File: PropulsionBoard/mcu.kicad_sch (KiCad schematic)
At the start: 22 parts, among them J3 Programming Header, U11 PIC18F26K83, U12 MC2562, Y1 Crystal

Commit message: Address Jack's comment on the propulsion board
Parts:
- removed IC1: ~, PropulsionBoard:QFN24_4MM_SMSC, symbol PropulsionBoard-eagle-import:PCF8575
- removed R42: 230R, Resistor_SMD:R_0805_2012Metric_Pad1.20x1.40mm_HandSolder, symbol Device:R_US
- removed R43, R44: 500R, Resistor_SMD:R_0805_2012Metric_Pad1.20x1.40mm_HandSolder, symbol Device:R_US
- added R13: 150R, Resistor_SMD:R_0805_2012Metric_Pad1.20x1.40mm_HandSolder, symbol Device:R_US
- added R14, R52: 330R, Resistor_SMD:R_0805_2012Metric_Pad1.20x1.40mm_HandSolder, symbol Device:R_US
- added U5: PCA9536DR, D8, symbol 2023-11-18_21-56-52:PCA9536DR
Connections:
- net +3V3: now also C17.2, J3.4 (Pin_4), R41.1, U11.20 (VDD), U12.5 (VIO), R13.1, R14.1, R52.1, U5.8 (VCC)
- net +5V: no longer C17.2, J3.4 (Pin_4), R41.1, U11.20 (VDD), U12.5 (VIO)
- net GND: now also U5.4 (GND)
- net SCL: now also U5.6 (SCL)
- net SDA: now also U5.7 (SDA)
- net at D1.2 (A): now also R13.2
- net at D2.2 (A): now also R14.2
- net at D3.2 (A): now also R52.2
- new net VALVE_CONTROL 1: U5.1 (P0)
- new net VALVE_CONTROL 2: U5.2 (P1)
- new net VALVE_CONTROL 3: U5.3 (P2)
- no-connect marks 0 -> 3

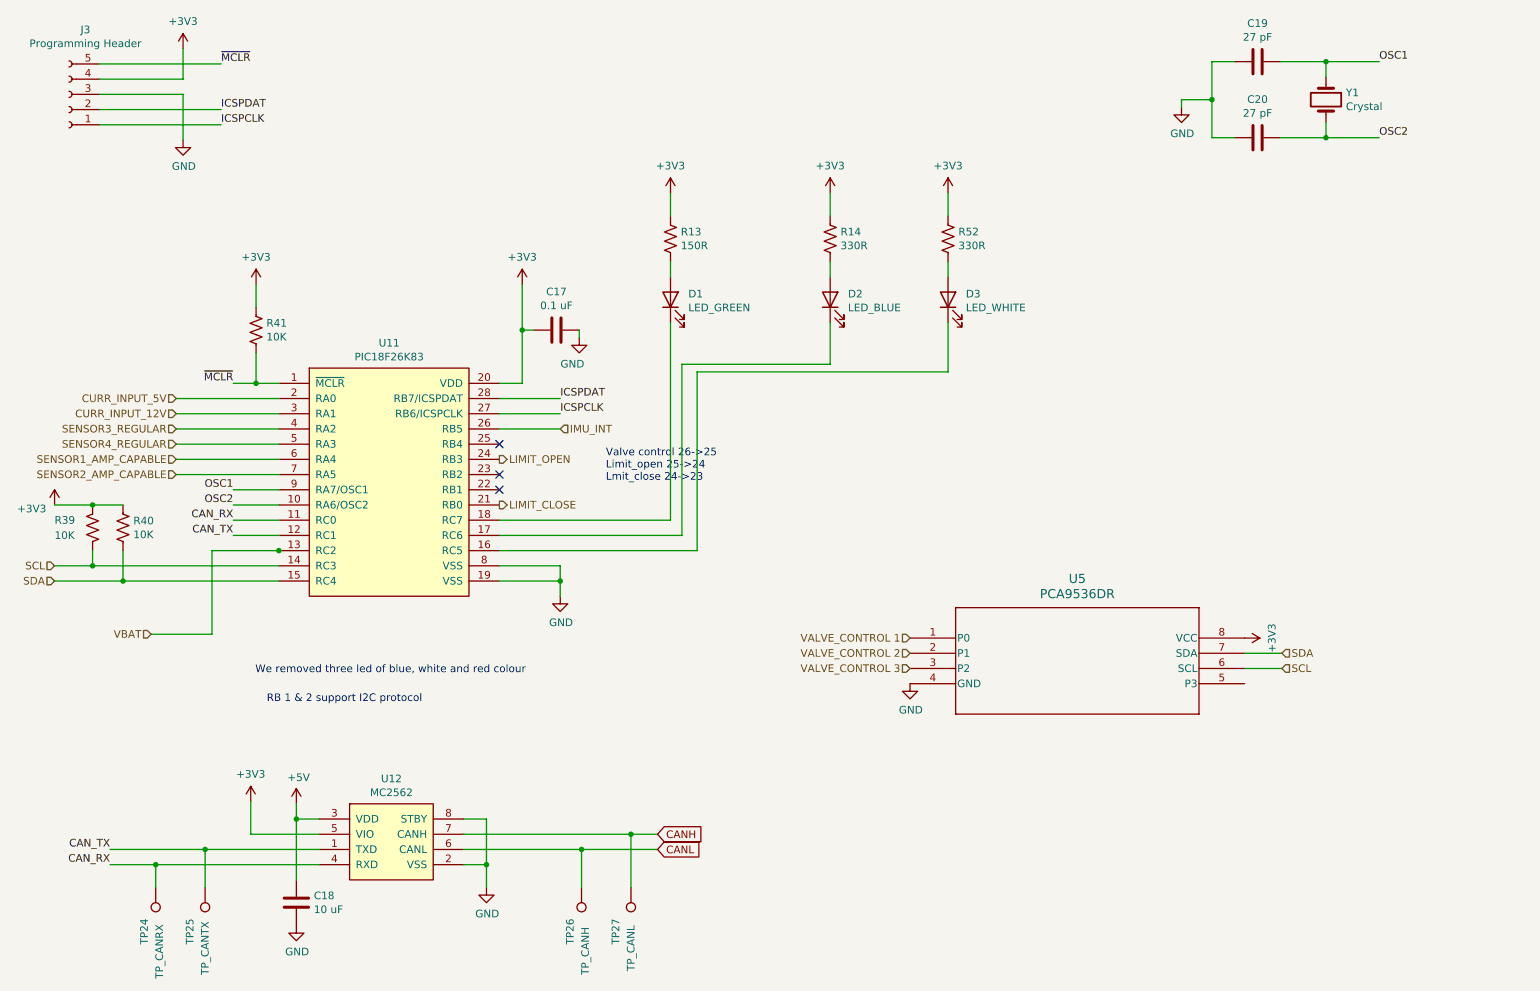
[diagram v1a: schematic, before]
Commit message: Propulsion Board Address Comments Final Revision
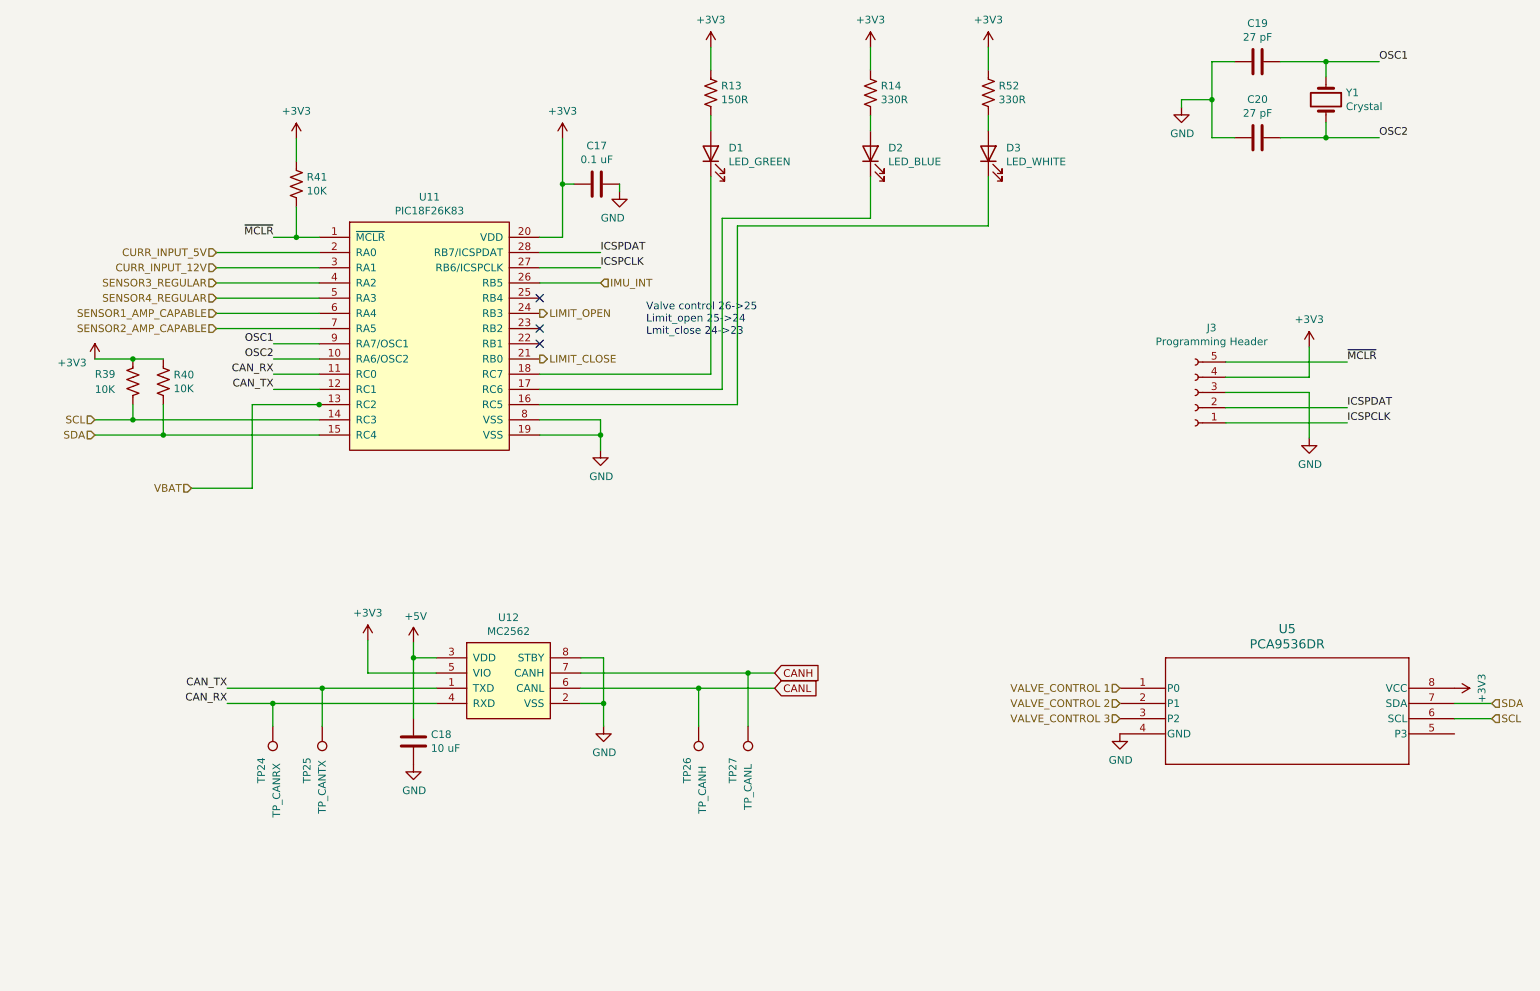
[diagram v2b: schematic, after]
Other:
- note removed: "RB 1 & 2 support I2C protocol"
- note removed: "We removed three led of blue, white and red colour"
- moved on the sheet: C17, C18, D1, D2, D3, J3, R13, R14, R39, R40, R41, R52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

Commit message: propulsion board address second review changes
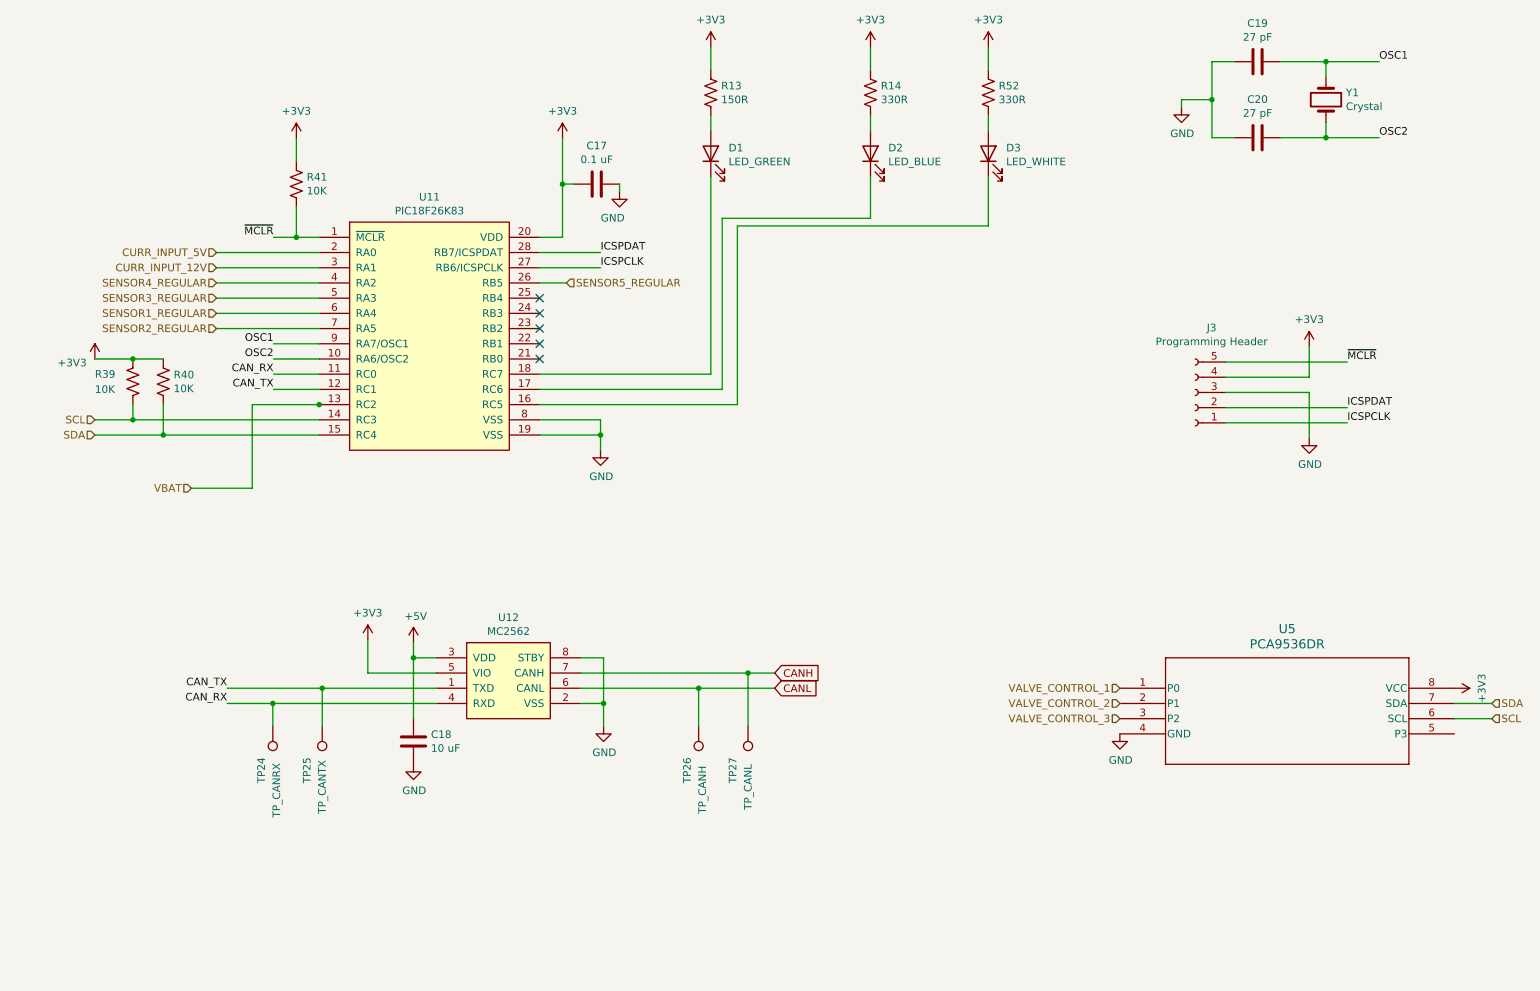
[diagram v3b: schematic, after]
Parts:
- U5: footprint D8 -> PCA9536DR:D8
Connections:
- net SENSOR3_REGULAR: now also U11.5 (RA3); no longer U11.4 (RA2)
- net SENSOR4_REGULAR: now also U11.4 (RA2); no longer U11.5 (RA3)
- net IMU_INT renamed SENSOR5_REGULAR
- net LIMIT_CLOSE: no longer names the net of U11.21 (RB0)
- net LIMIT_OPEN: no longer names the net of U11.24 (RB3)
- net SENSOR1_AMP_CAPABLE renamed SENSOR1_REGULAR
- net SENSOR2_AMP_CAPABLE renamed SENSOR2_REGULAR
- net VALVE_CONTROL 1 renamed VALVE_CONTROL_1
- net VALVE_CONTROL 2 renamed VALVE_CONTROL_2
- net VALVE_CONTROL 3 renamed VALVE_CONTROL_3
- no-connect marks 3 -> 5
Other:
- note removed: "Valve control 26->25 Limit_open 25->24 Lmit_close 24->23"
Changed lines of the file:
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@@
   (junction (at 48.641 95.758) (diameter 0) (color 0 0 0 0)
   )
+  (no_connect (at 111.506 83.058))
+  (no_connect (at 111.506 75.438))
   (no_connect (at 111.506 77.978))
   (no_connect (at 111.506 80.518))
@@
     (stroke (width 0) (type default))
   )
+  (wire (pts (xy 111.506 70.358) (xy 115.951 70.358))
+    (stroke (width 0) (type default))
+  )
   (wire (pts (xy 146.304 135.509) (xy 150.749 135.509))
     (stroke (width 0) (type default))
@@
     (stroke (width 0) (type default))
   )
-  (wire (pts (xy 111.506 70.358) (xy 121.666 70.358))
-    (stroke (width 0) (type default))
-  )
   (wire (pts (xy 166.751 52.578) (xy 166.751 59.563))
     (stroke (width 0) (type default))
@@
   (wire (pts (xy 242.824 46.101) (xy 242.824 43.561))
     (stroke (width 0) (type default))
-  )
-  (text "Valve control 26->25\nLimit_open 25->24\nLmit_close 24->23"
-    (at 129.286 79.248 0)
-    (effects (font (size 1.27 1.27)) (justify left bottom))
   )
   (label "ICSPDAT" (at 246.38 91.186 0) (fields_autoplaced)
@@
     )
   )
-  (hierarchical_label "SENSOR4_REGULAR" (shape input) (at 57.531 72.898 180) (fields_autoplaced)
+  (hierarchical_label "SENSOR3_REGULAR" (shape input) (at 57.531 72.898 180) (fields_autoplaced)
     (effects (font (size 1.27 1.27)) (justify right))
   )
@@
     (effects (font (size 1.27 1.27)) (justify right))
   )
-  (hierarchical_label "LIMIT_OPEN" (shape output) (at 111.506 75.438 0) (fields_autoplaced)
+  (hierarchical_label "SENSOR2_REGULAR" (shape input) (at 57.531 77.978 180) (fields_autoplaced)
+    (effects (font (size 1.27 1.27)) (justify right))
+  )
+  (hierarchical_label "SENSOR5_REGULAR" (shape input) (at 115.951 70.358 0) (fields_autoplaced)
     (effects (font (size 1.27 1.27)) (justify left))
   )
-  (hierarchical_label "SENSOR2_AMP_CAPABLE" (shape input) (at 57.531 77.978 180) (fields_autoplaced)
-    (effects (font (size 1.27 1.27)) (justify right))
-  )
-  (hierarchical_label "IMU_INT" (shape input) (at 121.666 70.358 0) (fields_autoplaced)
-    (effects (font (size 1.27 1.27)) (justify left))
-  )
-  (hierarchical_label "VALVE_CONTROL 1" (shape input) (at 208.407 138.049 180) (fields_autoplaced)
+  (hierarchical_label "VALVE_CONTROL_1" (shape input) (at 208.407 138.049 180) (fields_autoplaced)
     (effects (font (size 1.27 1.27)) (justify right))
   )
@@
     (effects (font (size 1.27 1.27)) (justify right))
   )
-  (hierarchical_label "LIMIT_CLOSE" (shape output) (at 111.506 83.058 0) (fields_autoplaced)
-    (effects (font (size 1.27 1.27)) (justify left))
-  )
-  (hierarchical_label "SENSOR1_AMP_CAPABLE" (shape input) (at 57.531 75.438 180) (fields_autoplaced)
+  (hierarchical_label "SENSOR1_REGULAR" (shape input) (at 57.531 75.438 180) (fields_autoplaced)
     (effects (font (size 1.27 1.27)) (justify right))
   )
@@
     (effects (font (size 1.27 1.27)) (justify right))
   )
-  (hierarchical_label "VALVE_CONTROL 3" (shape input) (at 208.407 143.129 180) (fields_autoplaced)
+  (hierarchical_label "VALVE_CONTROL_3" (shape input) (at 208.407 143.129 180) (fields_autoplaced)
     (effects (font (size 1.27 1.27)) (justify right))
   )
-  (hierarchical_label "VALVE_CONTROL 2" (shape input) (at 208.407 140.589 180) (fields_autoplaced)
+  (hierarchical_label "VALVE_CONTROL_2" (shape input) (at 208.407 140.589 180) (fields_autoplaced)
     (effects (font (size 1.27 1.27)) (justify right))
   )
@@
     (effects (font (size 1.27 1.27)) (justify right))
   )
-  (hierarchical_label "SENSOR3_REGULAR" (shape input) (at 57.531 70.358 180) (fields_autoplaced)
+  (hierarchical_label "SENSOR4_REGULAR" (shape input) (at 57.531 70.358 180) (fields_autoplaced)
     (effects (font (size 1.27 1.27)) (justify right))
   )
@@
       (effects (font (size 1.524 1.524)))
     )
-    (property "Footprint" "D8" (at 208.407 138.049 0)
+    (property "Footprint" "PCA9536DR:D8" (at 208.407 138.049 0)
       (effects (font (size 1.27 1.27) italic) hide)
     )

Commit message: addressing latest comments
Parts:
- removed D1: LED_GREEN, LED_SMD:LED_1206_3216Metric_Pad1.42x1.75mm_HandSolder, symbol Device:LED
- removed D2: LED_BLUE, LED_SMD:LED_1206_3216Metric_Pad1.42x1.75mm_HandSolder, symbol Device:LED
- removed D3: LED_WHITE, LED_SMD:LED_1206_3216Metric_Pad1.42x1.75mm_HandSolder, symbol Device:LED
- removed R13: 150R, Resistor_SMD:R_0805_2012Metric_Pad1.20x1.40mm_HandSolder, symbol Device:R_US
- removed R52: 330R, Resistor_SMD:R_0805_2012Metric_Pad1.20x1.40mm_HandSolder, symbol Device:R_US
- removed TP26: TP_CANH, sensor_mini:KEYSTONE_5000, symbol canhw:TestPointKeystone
- removed TP27: TP_CANL, sensor_mini:KEYSTONE_5000, symbol canhw:TestPointKeystone
- added C18: 0.1 uF, Capacitor_SMD:C_0805_2012Metric_Pad1.18x1.45mm_HandSolder, symbol Device:C
- added D1: LED_RED, LED_SMD:LED_1206_3216Metric_Pad1.42x1.75mm_HandSolder, symbol Device:LED
- added D1: LED_BLUE, LED_SMD:LED_1206_3216Metric_Pad1.42x1.75mm_HandSolder, symbol Device:LED
- added D1: LED_GREEN, LED_SMD:LED_1206_3216Metric_Pad1.42x1.75mm_HandSolder, symbol Device:LED
- added R22, R24: 130R, Resistor_SMD:R_0805_2012Metric_Pad1.20x1.40mm_HandSolder, symbol Device:R_US
- R14: value 330R -> 130R
- U5: footprint PCA9536DR:D8 -> Package_SO:SOIC-8_3.9x4.9mm_P1.27mm
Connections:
- net +3V3: now also R14.2, C18.1, R22.2, R24.2; no longer R14.1
- net GND: now also C18.2
- net SENSOR6: now reaches U11.21 (RB0)
- net SENSOR5: now reaches U11.22 (RB1)
- net SENSOR4: now reaches U11.23 (RB2)
- net SENSOR3: now reaches U11.24 (RB3)
- net SENSOR2: now reaches U11.25 (RB4)
- net SENSOR1_REGULAR renamed LED_RED
- net LED_RED: now also D1.1 (K)
- net SENSOR2_REGULAR: no longer names the net of U11.7 (RA5)
- net SENSOR3_REGULAR renamed LED_BLUE
- net LED_BLUE: now also D1.1 (K)
- net SENSOR4_REGULAR renamed LED_GREEN
- net LED_GREEN: now also D1.1 (K)
- net SENSOR5_REGULAR renamed SENSOR1
- new net: D1.2 (A), R22.1
- new net: D1.2 (A), R24.1
- new net: D1.2 (A), R14.1
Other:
- moved on the sheet: C17, C18, C19, C20, J3, R39, R40, R41, TP24, TP25, U11, U12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

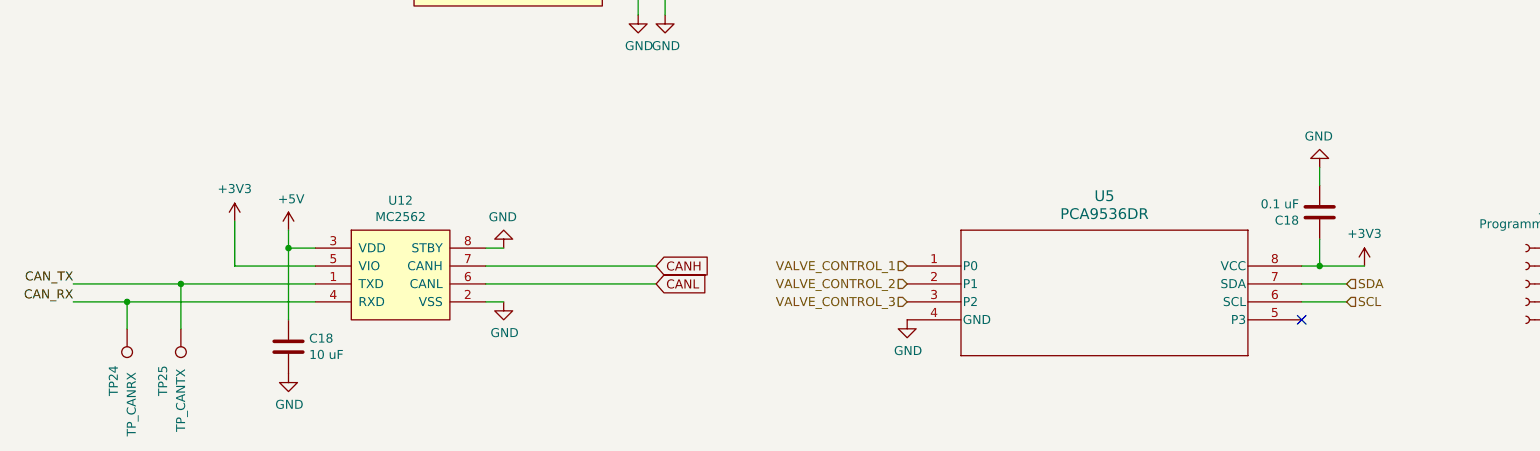
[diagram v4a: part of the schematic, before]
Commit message: propulsion board address forth review changes
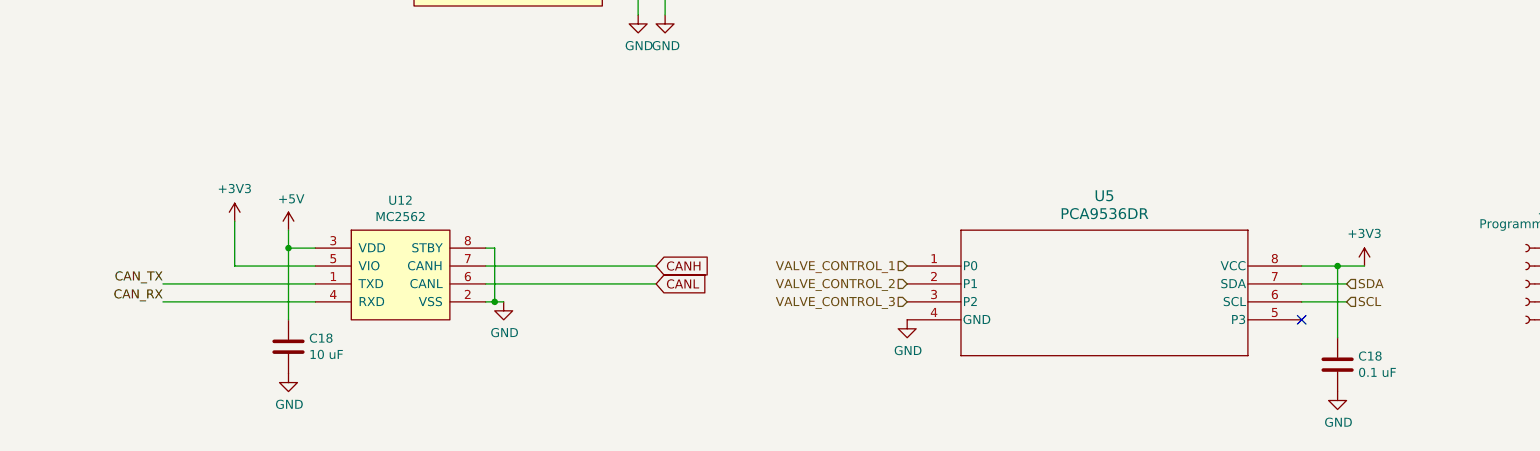
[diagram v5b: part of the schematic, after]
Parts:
- removed TP24: TP_CANRX, sensor_mini:KEYSTONE_5000, symbol canhw:TestPointKeystone
- removed TP25: TP_CANTX, sensor_mini:KEYSTONE_5000, symbol canhw:TestPointKeystone
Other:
- moved on the sheet: C18
